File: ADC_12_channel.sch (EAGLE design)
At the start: 163 parts, among them IC1 LM317BD2T, IC2 LM317BD2T, K1 691131710003, K2 691101710002, K3 691101710002, K4 691101710002, K5 691101710002, K6 691101710002, K7 691101710002, K8 691101710002, K9 691101710002, U1 AD7864ASZ-1, U10 TL082D, U12 V_REG_317SMD, U2 AD7864ASZ-1, U3 TL082D, U4 TL082D, U5 TL082D, U6 TL082D, U7 TL082D, U8 TL082D, U9 TL082D, X1 QTE-040

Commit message: Supply Finally sorted out!
arranging supply components
Working on realigning resistors of input stage
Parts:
- added R75: 100k, rcl:R-EU_R1206
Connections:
- removed net 0.8V: R21.2, R22.1, R23.1
- new net 3V: R21.2, R22.1, R23.1, R75.2
- net VCC_5+: now also R75.1
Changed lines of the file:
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@@
 <grid distance="0.1" unitdist="inch" unit="inch" style="lines" multiple="1" display="no" altdistance="0.01" altunitdist="inch" altunit="inch"/>
 <layers>
-<layer number="1" name="Top" color="4" fill="1" visible="yes" active="no"/>
-<layer number="2" name="Route2" color="1" fill="3" visible="yes" active="no"/>
-<layer number="3" name="Route3" color="4" fill="3" visible="yes" active="no"/>
-<layer number="4" name="Route4" color="1" fill="4" visible="yes" active="no"/>
-<layer number="5" name="Route5" color="4" fill="4" visible="yes" active="no"/>
-<layer number="6" name="Route6" color="1" fill="8" visible="yes" active="no"/>
-<layer number="7" name="Route7" color="4" fill="8" visible="yes" active="no"/>
-<layer number="8" name="Route8" color="1" fill="2" visible="yes" active="no"/>
-<layer number="9" name="Route9" color="4" fill="2" visible="yes" active="no"/>
-<layer number="10" name="Route10" color="1" fill="7" visible="yes" active="no"/>
-<layer number="11" name="Route11" color="4" fill="7" visible="yes" active="no"/>
-<layer number="12" name="Route12" color="1" fill="5" visible="yes" active="no"/>
-<layer number="13" name="Route13" color="4" fill="5" visible="yes" active="no"/>
-<layer number="14" name="Route14" color="1" fill="6" visible="yes" active="no"/>
-<layer number="15" name="Route15" color="4" fill="6" visible="yes" active="no"/>
-<layer number="16" name="Bottom" color="1" fill="1" visible="yes" active="no"/>
-<layer number="17" name="Pads" color="2" fill="1" visible="yes" active="no"/>
-<layer number="18" name="Vias" color="2" fill="1" visible="yes" active="no"/>
-<layer number="19" name="Unrouted" color="6" fill="1" visible="yes" active="no"/>
-<layer number="20" name="Dimension" color="15" fill="1" visible="yes" active="no"/>
-<layer number="21" name="tPlace" color="7" fill="1" visible="yes" active="no"/>
-<layer number="22" name="bPlace" color="7" fill="1" visible="yes" active="no"/>
-<layer number="23" name="tOrigins" color="15" fill="1" visible="yes" active="no"/>
-<layer number="24" name="bOrigins" color="15" fill="1" visible="yes" active="no"/>
-<layer number="25" name="tNames" color="7" fill="1" visible="yes" active="no"/>
-<layer number="26" name="bNames" color="7" fill="1" visible="yes" active="no"/>
-<layer number="27" name="tValues" color="7" fill="1" visible="yes" active="no"/>
-<layer number="28" name="bValues" color="7" fill="1" visible="yes" active="no"/>
+<layer number="1" name="Top" color="4" fill="1" visible="no" active="no"/>
+<layer number="2" name="Route2" color="1" fill="3" visible="no" active="no"/>
+<layer number="3" name="Route3" color="4" fill="3" visible="no" active="no"/>
+<layer number="4" name="Route4" color="1" fill="4" visible="no" active="no"/>
+<layer number="5" name="Route5" color="4" fill="4" visible="no" active="no"/>
+<layer number="6" name="Route6" color="1" fill="8" visible="no" active="no"/>
+<layer number="7" name="Route7" color="4" fill="8" visible="no" active="no"/>
+<layer number="8" name="Route8" color="1" fill="2" visible="no" active="no"/>
+<layer number="9" name="Route9" color="4" fill="2" visible="no" active="no"/>
+<layer number="10" name="Route10" color="1" fill="7" visible="no" active="no"/>
+<layer number="11" name="Route11" color="4" fill="7" visible="no" active="no"/>
+<layer number="12" name="Route12" color="1" fill="5" visible="no" active="no"/>
+<layer number="13" name="Route13" color="4" fill="5" visible="no" active="no"/>
+<layer number="14" name="Route14" color="1" fill="6" visible="no" active="no"/>
+<layer number="15" name="Route15" color="4" fill="6" visible="no" active="no"/>
+<layer number="16" name="Bottom" color="1" fill="1" visible="no" active="no"/>
+<layer number="17" name="Pads" color="2" fill="1" visible="no" active="no"/>
+<layer number="18" name="Vias" color="2" fill="1" visible="no" active="no"/>
+<layer number="19" name="Unrouted" color="6" fill="1" visible="no" active="no"/>
+<layer number="20" name="Dimension" color="15" fill="1" visible="no" active="no"/>
+<layer number="21" name="tPlace" color="7" fill="1" visible="no" active="no"/>
+<layer number="22" name="bPlace" color="7" fill="1" visible="no" active="no"/>
+<layer number="23" name="tOrigins" color="15" fill="1" visible="no" active="no"/>
+<layer number="24" name="bOrigins" color="15" fill="1" visible="no" active="no"/>
+<layer number="25" name="tNames" color="7" fill="1" visible="no" active="no"/>
+<layer number="26" name="bNames" color="7" fill="1" visible="no" active="no"/>
+<layer number="27" name="tValues" color="7" fill="1" visible="no" active="no"/>
+<layer number="28" name="bValues" color="7" fill="1" visible="no" active="no"/>
 <layer number="29" name="tStop" color="7" fill="3" visible="no" active="no"/>
 <layer number="30" name="bStop" color="7" fill="6" visible="no" active="no"/>
@@
 <layer number="35" name="tGlue" color="7" fill="4" visible="no" active="no"/>
 <layer number="36" name="bGlue" color="7" fill="5" visible="no" active="no"/>
-<layer number="37" name="tTest" color="7" fill="1" visible="yes" active="no"/>
-<layer number="38" name="bTest" color="7" fill="1" visible="yes" active="no"/>
+<layer number="37" name="tTest" color="7" fill="1" visible="no" active="no"/>
+<layer number="38" name="bTest" color="7" fill="1" visible="no" active="no"/>
 <layer number="39" name="tKeepout" color="4" fill="11" visible="no" active="no"/>
 <layer number="40" name="bKeepout" color="1" fill="11" visible="no" active="no"/>
@@
 <layer number="44" name="Drills" color="7" fill="1" visible="no" active="no"/>
 <layer number="45" name="Holes" color="7" fill="1" visible="no" active="no"/>
-<layer number="46" name="Milling" color="3" fill="1" visible="yes" active="no"/>
-<layer number="47" name="Measures" color="7" fill="1" visible="yes" active="no"/>
-<layer number="48" name="Document" color="7" fill="1" visible="yes" active="no"/>
-<layer number="49" name="Reference" color="7" fill="1" visible="yes" active="no"/>
-<layer number="50" name="dxf" color="7" fill="1" visible="yes" active="no"/>
-<layer number="51" name="tDocu" color="7" fill="1" visible="yes" active="no"/>
-<layer number="52" name="bDocu" color="7" fill="1" visible="yes" active="no"/>
-<layer number="53" name="tGND_GNDA" color="7" fill="9" visible="yes" active="no"/>
-<layer number="54" name="bGND_GNDA" color="1" fill="9" visible="yes" active="no"/>
-<layer number="56" name="wert" color="7" fill="1" visible="yes" active="no"/>
-<layer number="57" name="tCAD" color="7" fill="1" visible="yes" active="no"/>
-<layer number="59" name="tCarbon" color="7" fill="1" visible="yes" active="no"/>
-<layer number="60" name="bCarbon" color="7" fill="1" visible="yes" active="no"/>
+<layer number="46" name="Milling" color="3" fill="1" visible="no" active="no"/>
+<layer number="47" name="Measures" color="7" fill="1" visible="no" active="no"/>
+<layer number="48" name="Document" color="7" fill="1" visible="no" active="no"/>
+<layer number="49" name="Reference" color="7" fill="1" visible="no" active="no"/>
+<layer number="50" name="dxf" color="7" fill="1" visible="no" active="no"/>
+<layer number="51" name="tDocu" color="7" fill="1" visible="no" active="no"/>
+<layer number="52" name="bDocu" color="7" fill="1" visible="no" active="no"/>
+<layer number="53" name="tGND_GNDA" color="7" fill="9" visible="no" active="no"/>
+<layer number="54" name="bGND_GNDA" color="1" fill="9" visible="no" active="no"/>
+<layer number="56" name="wert" color="7" fill="1" visible="no" active="no"/>
+<layer number="57" name="tCAD" color="7" fill="1" visible="no" active="no"/>
+<layer number="59" name="tCarbon" color="7" fill="1" visible="no" active="no"/>
+<layer number="60" name="bCarbon" color="7" fill="1" visible="no" active="no"/>
 <layer number="90" name="Modules" color="5" fill="1" visible="yes" active="yes"/>
 <layer number="91" name="Nets" color="2" fill="1" visible="yes" active="yes"/>
@@
 <part name="IC2" library="v-reg" deviceset="LM317?*" device="BD2T"/>
 <part name="R74" library="resistor" deviceset="R-EU_" device="M1206" value="0"/>
+<part name="R75" library="rcl" deviceset="R-EU_" device="R1206" value="100k"/>
 </parts>
 <sheets>
@@
 <instance part="IC2" gate="G$1" x="617.22" y="274.32"/>
 <instance part="R74" gate="G$1" x="-33.02" y="63.5" rot="R180"/>
+<instance part="R75" gate="G$1" x="731.52" y="276.86" rot="R270"/>
 </instances>
 <busses>
@@
 <pinref part="R21" gate="G$1" pin="1"/>
 <wire x1="701.04" y1="292.1" x2="736.6" y2="292.1" width="0.1524" layer="91"/>
-<wire x1="736.6" y1="292.1" x2="736.6" y2="281.94" width="0.1524" layer="91"/>
+<wire x1="736.6" y1="292.1" x2="736.6" y2="287.02" width="0.1524" layer="91"/>
 <pinref part="U12" gate="G$1" pin="OUT"/>
-</segment>
-</net>
-<net name="0.8V" class="0">
+<pinref part="R75" gate="G$1" pin="1"/>
+<wire x1="736.6" y1="287.02" x2="736.6" y2="281.94" width="0.1524" layer="91"/>
+<wire x1="731.52" y1="281.94" x2="731.52" y2="287.02" width="0.1524" layer="91"/>
+<wire x1="731.52" y1="287.02" x2="736.6" y2="287.02" width="0.1524" layer="91"/>
+<junction x="736.6" y="287.02"/>
+</segment>
+</net>
+<net name="3V" class="0">
 <segment>
 <pinref part="R21" gate="G$1" pin="2"/>
@@
 <wire x1="731.52" y1="266.7" x2="731.52" y2="269.24" width="0.1524" layer="91"/>
 <wire x1="731.52" y1="269.24" x2="736.6" y2="269.24" width="0.1524" layer="91"/>
-</segment>
-</net>
+<pinref part="R75" gate="G$1" pin="2"/>
+<wire x1="731.52" y1="271.78" x2="731.52" y2="269.24" width="0.1524" layer="91"/>
+<junction x="731.52" y="269.24"/>
+<label x="739.14" y="269.24" size="1.778" layer="95" xref="yes"/>
+</segment>
+</net>

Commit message: Layout of Supply DONE!
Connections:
- removed net GND2: C20.-, C21.+, C22.1, C24.-, C25.+, C26.2, C28.-, C59.2, IC1.ADJ, IC2.ADJ, K1.2, LED5.C, LED6.C, LED7.C, R22.2, R23.2, R73.1, U12.ADJ
- net DGND: now also C20.-, C21.+, C22.1, C24.-, C25.+, C26.2, C28.-, C59.2, IC1.ADJ, IC2.ADJ, K1.2, LED5.C, LED6.C, LED7.C, R22.2, R23.2, R73.1, U12.ADJ

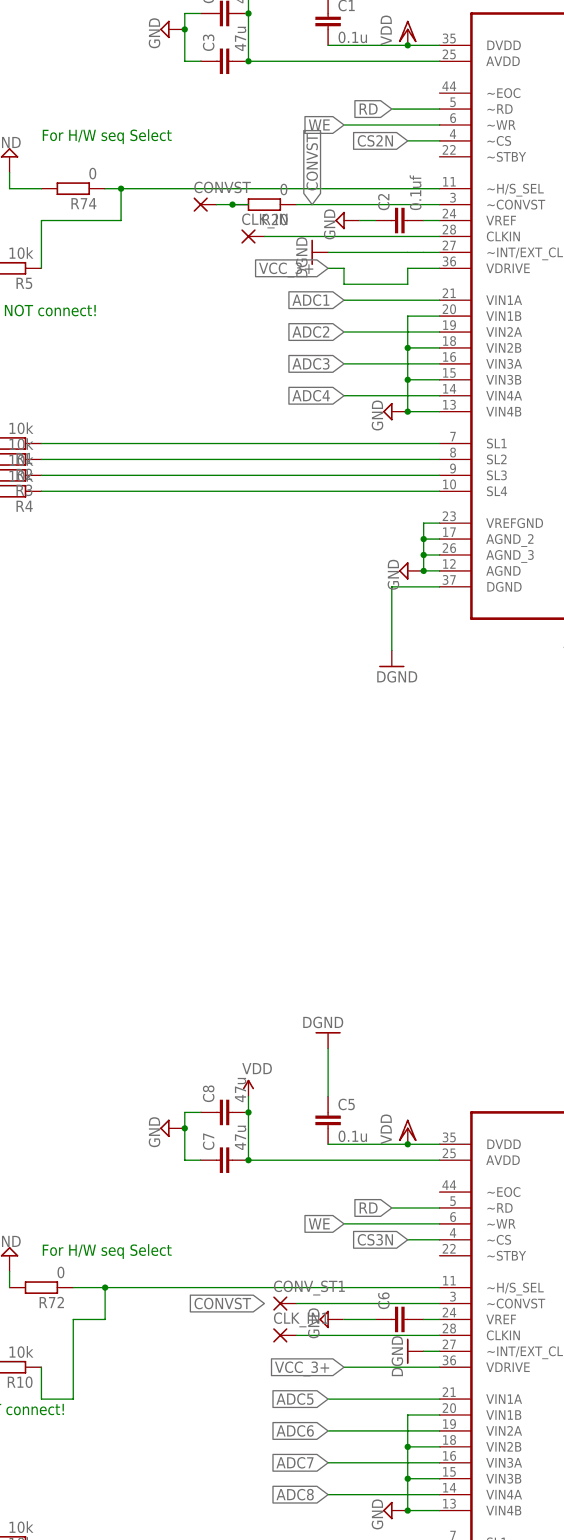
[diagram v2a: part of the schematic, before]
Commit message: Conversion ST signal, supply & area
-Added isolating resistor in CONVST signal coming from header/processor
-Defined boundry of the baord
- Relocated and reorianted the supply
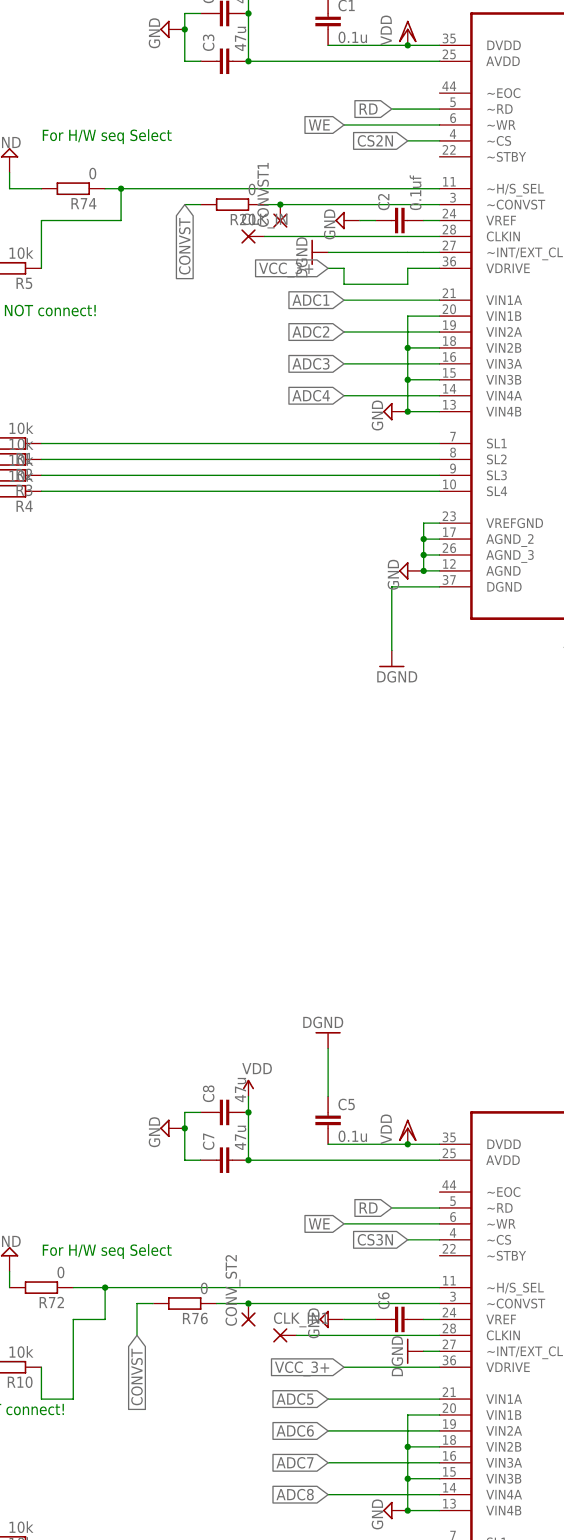
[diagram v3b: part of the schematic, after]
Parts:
- removed CONVST, CONV_ST1: (no value), wirepad:3,17/1,3
- added CONVST1, CONV_ST2: (no value), wirepad:3,17/1,3
- added R76: 0, resistor:R-EU_M1206
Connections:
- removed net N$42: CONVST.P, R20.2
- new net N$18: CONVST1.P, R20.1, U1.~CONVST
- new net N$25: CONV_ST2.P, R76.1, U2.~CONVST
- net CONVST: now also R20.2, R76.2; no longer CONV_ST1.P, R20.1, U1.~CONVST, U2.~CONVST
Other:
- moved on the sheet: R20
